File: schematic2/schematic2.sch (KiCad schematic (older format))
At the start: 47 parts, among them J1 Barrel_Jack, K1 TIANBO_HJR_1-2C, P1 Conn_02x20_Odd_Even, Q1 BC547, Q2 DMP1045U, Q3 BC547, Q4 BC547, Q5 BC547, U1 buck, U3 LM317_SOT-223

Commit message: Remove un-needed FET.
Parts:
- removed Q2: DMP1045U, Package_TO_SOT_SMD:SOT-23, symbol Device:Q_PMOS_GDS
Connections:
- wire segments 187 -> 182
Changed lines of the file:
@@
 	1    0    0    -1
 $EndComp
-Wire Wire Line
-	5850 3100 5950 3100
 $Comp
 L Mikes:buck U1
@@
 	1    0    0    -1
 $EndComp
-Wire Wire Line
-	6150 2800 6150 1350
-Wire Wire Line
-	6150 1350 4400 1350
-Wire Wire Line
-	4400 1350 4400 1650
-Connection ~ 4400 1650
-Wire Wire Line
-	4400 1650 4650 1650
-$Comp
-L Device:Q_PMOS_GDS Q2
-U 1 1 5F0952D9
-P 6150 3000
-F 0 "Q2" V 6399 2797 50  0000 L CNN
-F 1 "DMP1045U" V 6490 2797 50  0000 L CNN
-F 2 "Package_TO_SOT_SMD:SOT-23" H 6350 3100 50  0001 C CNN
-F 3 "~" H 6150 3000 50  0001 C CNN
-	1    6150 3000
-	0    -1   1    0
-$EndComp
 $Comp
 L Regulator_Linear:LM317_SOT-223 U?
@@
 	4150 3100 4150 3050
 Wire Wire Line
-	6350 3100 6700 3100
-Wire Wire Line
 	4950 1650 6300 1650
 Connection ~ 2650 1650
-Wire Wire Line
-	2650 1650 4400 1650
 $Comp
 L Diode:1N4001 D15
@@
 Wire Wire Line
 	4450 3550 4800 3550
+Wire Wire Line
+	5850 3100 6700 3100
+Wire Wire Line
+	2650 1650 4650 1650
 $EndSCHEMATC

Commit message: Boards ordered.
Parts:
- added J2: Conn_01x02, Connector_Molex:Molex_KK-254_AE-6410-02A_1x02_P2.54mm_Vertical, symbol Connector_Generic:Conn_01x02
- added R16: 1K, Resistor_THT:R_Axial_DIN0204_L3.6mm_D1.6mm_P5.08mm_Horizontal, symbol Device:R
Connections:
- net GND: now also J2.1 (Pin_1)
- net GPIO17(GEN0) renamed GPIO17
- net GPIO17: now also R16.1
- new net: J2.2 (Pin_2), R16.2
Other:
- note added: "POTENTIALLY USEFUL\nBUTTON ? :)"
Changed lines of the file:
@@
 Sheet 1 2
 Title "LiPo Pi UPS"
-Date "2020-06-03"
-Rev "2 DEV"
+Date "2021-08-11"
+Rev "3"
 Comp "MILLSTREAM COMPUTING"
 Comment1 ""
@@
 Wire Notes Line
 	3350 3900 3350 6200
-Wire Notes Line
-	3350 6200 9150 6200
-Wire Notes Line
-	9150 6200 9150 3900
-Wire Notes Line
-	9150 3900 3350 3900
 Text Notes 3400 4000 0    50   ~ 0
 Power Fail Detection
@@
 	6000 1500 6000 3450
 Wire Notes Line
-	6000 3450 9300 3450
-Wire Notes Line
 	9300 3450 9300 1500
 Wire Notes Line
@@
 Wire Wire Line
 	2650 1650 4650 1650
+Wire Notes Line
+	3350 3900 7100 3900
+Wire Notes Line
+	7100 3900 7100 6200
+Wire Notes Line
+	7100 6200 3350 6200
+Wire Notes Line
+	6000 3450 7250 3450
+Wire Notes Line
+	7250 3450 7250 4950
+Wire Notes Line
+	7250 4950 9900 4950
+Wire Notes Line
+	9900 4950 9900 3450
+Wire Notes Line
+	9900 3450 9300 3450
+Text GLabel -4300 3300 0    50   Input ~ 0
+GPIO17
+Text GLabel 10000 5550 2    50   Input ~ 0
+GPIO17
+$Comp
+L Connector_Generic:Conn_01x02 J2
+U 1 1 611A8E2F
+P 9250 5650
+F 0 "J2" H 9168 5325 50  0000 C CNN
+F 1 "Conn_01x02" H 9168 5416 50  0000 C CNN
+F 2 "Connector_Molex:Molex_KK-254_AE-6410-02A_1x02_P2.54mm_Vertical" H 9250 5650 50  0001 C CNN
+F 3 "~" H 9250 5650 50  0001 C CNN
+	1    9250 5650
+	-1   0    0    1
+$EndComp
+$Comp
+L power:GND #PWR0104
+U 1 1 611A94D4
+P 9450 5850
+F 0 "#PWR0104" H 9450 5600 50  0001 C CNN
+F 1 "GND" H 9450 5700 50  0000 C CNN
+F 2 "" H 9450 5850 50  0001 C CNN
+F 3 "" H 9450 5850 50  0001 C CNN
+	1    9450 5850
+	1    0    0    -1
+$EndComp
+$Comp
+L Device:R R16
+U 1 1 611A9DB8
+P 9750 5550
+F 0 "R16" V 9830 5550 50  0000 C CNN
+F 1 "1K" V 9750 5550 50  0000 C CNN
+F 2 "Resistor_THT:R_Axial_DIN0204_L3.6mm_D1.6mm_P5.08mm_Horizontal" V 9680 5550 50  0001 C CNN
+F 3 "" H 9750 5550 50  0001 C CNN
+	1    9750 5550
+	0    1    1    0
+$EndComp
+Wire Wire Line
+	9450 5550 9600 5550
+Wire Wire Line
+	9900 5550 10000 5550
+Wire Wire Line
+	9450 5650 9450 5850
+Text Notes 9600 5850 0    50   ~ 0
+POTENTIALLY USEFUL\nBUTTON ? :)
 $EndSCHEMATC

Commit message: Detail changes made from release note.
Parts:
- removed D14: 1N4001, Diode_SMD:D_2010_5025Metric, symbol Diode:1N4001
- removed K1: TIANBO_HJR_1-2C, Mikee:Relay_DPDT_HJR_1-2C, symbol Mikes:TIANBO_HJR_1-2C
- added Q2: FDS9435A, Package_SO:SOIC-8_3.9x4.9mm_P1.27mm, symbol Transistor_FET:FDS9435A
- added R17: 10K, Resistor_THT:R_Axial_DIN0204_L3.6mm_D1.6mm_P5.08mm_Horizontal, symbol Device:R
- BT1, BT2: value Battery_Cell -> 302323 LiPo
- C3: footprint Capacitor_SMD:C_0805_2012Metric -> Capacitor_SMD:C_1206_3216Metric
- D12: footprint Resistor_THT:R_Axial_DIN0207_L6.3mm_D2.5mm_P7.62mm_Horizontal -> Diode_THT:D_A-405_P7.62mm_Horizontal
- D3: value 5V6 -> 5V1
- D9: value 1N4001 -> 1N4148; footprint Diode_SMD:D_2010_5025Metric -> Diode_THT:D_DO-41_SOD81_P7.62mm_Horizontal
- R15: value 320R -> 310R
- R6: value 8K2 -> 10K
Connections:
- net +5V: no longer D9.1 (K)
- net at D11.1 (K), Q4.1 (C): now also Q2.4 (G), R17.2; no longer D9.2 (A)
- net at D7.1 (K): now also Q2.1 (S), Q2.2 (S), Q2.3 (S), R17.1
- net at D5.1 (K), U1.1 (V+in): now also Q2.5 (D), Q2.6 (D), Q2.7 (D), Q2.8 (D)
- net at C1.1, U3.3 (VI): now also D9.1 (K)
- net +9V renamed +12V
- net +12V: now also D9.2 (A)
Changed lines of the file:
@@
 Sheet 1 2
 Title "LiPo Pi UPS"
-Date "2021-08-11"
-Rev "3"
+Date "2022-04-04"
+Rev "3.1"
 Comp "MILLSTREAM COMPUTING"
-Comment1 ""
-Comment2 ""
+Comment1 "NOT FOR MANUFACTURE"
+Comment2 "SEE HW RELEASE NOT 101 FOR V3 FOR CHANGES"
 Comment3 ""
 Comment4 ""
@@
 $EndComp
 $Comp
-L power:+9V #PWR06
-U 1 1 5B3B4742
-P 1800 1350
-F 0 "#PWR06" H 1800 1200 50  0001 C CNN
-F 1 "+9V" H 1800 1490 50  0000 C CNN
-F 2 "" H 1800 1350 50  0001 C CNN
-F 3 "" H 1800 1350 50  0001 C CNN
-	1    1800 1350
-	1    0    0    -1
-$EndComp
-$Comp
-L Diode:1N4001 D9
-U 1 1 5B3B47EF
-P 7900 2750
-F 0 "D9" H 7900 2850 50  0000 C CNN
-F 1 "1N4001" H 7900 2650 50  0000 C CNN
-F 2 "Diode_SMD:D_2010_5025Metric" H 7900 2575 50  0001 C CNN
-F 3 "" H 7900 2750 50  0001 C CNN
-	1    7900 2750
-	0    1    1    0
-$EndComp
-$Comp
 L Diode:1N4001 D7
 U 1 1 5B3B494C
@@
 P 4600 5800
 F 0 "R6" V 4680 5800 50  0000 C CNN
-F 1 "8K2" V 4600 5800 50  0000 C CNN
+F 1 "10K" V 4600 5800 50  0000 C CNN
 F 2 "Resistor_THT:R_Axial_DIN0204_L3.6mm_D1.6mm_P5.08mm_Horizontal" V 4530 5800 50  0001 C CNN
 F 3 "" H 4600 5800 50  0001 C CNN
@@
 	1700 1850 1700 2050
 Connection ~ 1800 1650
-Wire Wire Line
-	6300 2450 6300 1650
 $Comp
 L power:GND #PWR09
@@
 $EndComp
 Wire Wire Line
-	7700 1650 7700 2450
-Wire Wire Line
-	7700 2450 7500 2450
-Wire Wire Line
-	7700 2450 7900 2450
-Wire Wire Line
-	7900 2450 7900 2600
-Connection ~ 7700 2450
-Wire Wire Line
-	7500 3050 7500 3200
-Wire Wire Line
-	7500 3200 7900 3200
-Wire Wire Line
-	7900 3200 7900 2900
-Connection ~ 7500 3200
-Wire Wire Line
-	7500 3200 7500 3500
-Wire Wire Line
 	8200 4250 7800 4250
 Wire Wire Line
@@
 Wire Wire Line
 	7500 6050 7500 6250
-Wire Wire Line
-	7700 1650 8300 1650
 Wire Wire Line
 	10350 1650 10350 1250
@@
 P 2100 3400
 F 0 "D3" H 2100 3500 50  0000 C CNN
-F 1 "5V6" H 2100 3300 50  0000 C CNN
+F 1 "5V1" H 2100 3300 50  0000 C CNN
 F 2 "Diode_THT:D_A-405_P7.62mm_Horizontal" H 2100 3400 50  0001 C CNN
 F 3 "~" H 2100 3400 50  0001 C CNN
@@
 Connection ~ 6300 1650
 Wire Wire Line
-	7450 1650 7700 1650
-Wire Wire Line
 	6700 1950 6700 2050
-Connection ~ 7700 1650
 Text Notes 5400 4750 0    50   ~ 0
 0=OK, 1=POWER FAIL
@@
 Text Notes 1950 3750 1    50   ~ 0
 POWER INDICATOR
-Text Notes 8350 2900 0    50   ~ 0
+Text Notes 8450 3100 0    50   ~ 0
 UPS ACTIVE\nINDICATOR
 Text Notes 6250 4450 0    50   ~ 0
@@
 F 0 "C3" H 4565 2796 50  0000 L CNN
 F 1 "100n" H 4565 2705 50  0000 L CNN
-F 2 "Capacitor_SMD:C_0805_2012Metric" H 4488 2600 50  0001 C CNN
+F 2 "Capacitor_SMD:C_1206_3216Metric" H 4488 2600 50  0001 C CNN
 F 3 "~" H 4450 2750 50  0001 C CNN
 	1    4450 2750
@@
 AR Path="/5F2C0373" Ref="BT1"  Part="1"
 F 0 "BT1" H 5268 2596 50  0000 L CNN
-F 1 "Battery_Cell" H 5268 2505 50  0000 L CNN
+F 1 "302323 LiPo" H 5268 2505 50  0000 L CNN
 F 2 "Connector_Molex:Molex_KK-254_AE-6410-02A_1x02_P2.54mm_Vertical" V 5150 2560 50  0001 C CNN
 F 3 "~" V 5150 2560 50  0001 C CNN
@@
 AR Path="/5F2C0379" Ref="BT2"  Part="1"
 F 0 "BT2" H 5268 3396 50  0000 L CNN
-F 1 "Battery_Cell" H 5268 3305 50  0000 L CNN
+F 1 "302323 LiPo" H 5268 3305 50  0000 L CNN
 F 2 "Connector_Molex:Molex_KK-254_AE-6410-02A_1x02_P2.54mm_Vertical" V 5150 3360 50  0001 C CNN
 F 3 "~" V 5150 3360 50  0001 C CNN
@@
 F 0 "D12" V 4754 3202 50  0000 C CNN
 F 1 "3V6" V 4845 3202 50  0000 C CNN
-F 2 "Resistor_THT:R_Axial_DIN0207_L6.3mm_D2.5mm_P7.62mm_Horizontal" H 4800 3050 50  0001 C CNN
+F 2 "Diode_THT:D_A-405_P7.62mm_Horizontal" H 4800 3050 50  0001 C CNN
 F 3 "~" H 4800 3050 50  0001 C CNN
 	1    4800 3050
@@
 Connection ~ 2800 2150
 Wire Wire Line
-	2100 1650 2650 1650
-Wire Wire Line
 	2100 6050 3800 6050
-Wire Wire Line
-	2650 1650 2650 1750
 Wire Wire Line
 	5150 3550 5550 3550
@@
 AR Path="/5F3B4ACA" Ref="R15"  Part="1"
 F 0 "R15" H 4319 3296 50  0000 C CNN
-F 1 "320R" H 4319 3205 50  0000 C CNN
+F 1 "310R" H 4319 3205 50  0000 C CNN
 F 2 "Resistor_THT:R_Axial_DIN0204_L3.6mm_D1.6mm_P5.08mm_Horizontal" V 4080 3250 50  0001 C CNN
 F 3 "~" H 4150 3250 50  0001 C CNN
@@
 Wire Wire Line
 	4950 1650 6300 1650
-Connection ~ 2650 1650
 $Comp
 L Diode:1N4001 D15
@@
 Wire Wire Line
 	5850 3550 6000 3550
-$Comp
-L Diode:1N4001 D14
-U 1 1 5F3EA42D
-P 2650 1900
-F 0 "D14" H 2650 2000 50  0000 C CNN
-F 1 "1N4001" H 2650 1800 50  0000 C CNN
-F 2 "Diode_SMD:D_2010_5025Metric" H 2650 1725 50  0001 C CNN
-F 3 "" H 2650 1900 50  0001 C CNN
-	1    2650 1900
-	0    -1   -1   0
-$EndComp
-Wire Wire Line
-	2650 2050 2650 2150
-$Comp
-L Mikes:TIANBO_HJR_1-2C K1
-U 1 1 5F44ADD7
-P 7300 2750
-F 0 "K1" H 6181 2796 50  0000 L CNN
-F 1 "TIANBO_HJR_1-2C" H 6181 2705 50  0000 L CNN
-F 2 "Mikee:Relay_DPDT_HJR_1-2C" H 8850 2720 50  0001 C CNN
-F 3 "" H 7300 2750 50  0001 C CNN
-	1    7300 2750
-	-1   0    0    -1
-$EndComp
+Wire Wire Line
+	2650 1650 2650 1750
 Wire Wire Line
 	6300 2450 6600 2450
 Wire Wire Line
-	6700 3050 6700 3100
+	6600 2850 6600 3100
 Text GLabel 2750 6650 2    50   Input ~ 0
 CLK_BAT
@@
 	4450 3550 4800 3550
 Wire Wire Line
-	5850 3100 6700 3100
-Wire Wire Line
-	2650 1650 4650 1650
+	5850 3100 6150 3100
 Wire Notes Line
 	3350 3900 7100 3900
@@
 Text Notes 9600 5850 0    50   ~ 0
 POTENTIALLY USEFUL\nBUTTON ? :)
+Wire Wire Line
+	2100 1650 2650 1650
+Connection ~ 2650 1650
+Wire Wire Line
+	2650 1650 4650 1650
+$Comp
+L power:+12V #PWR0105
+U 1 1 624FAA52
+P 1800 1350
+F 0 "#PWR0105" H 1800 1200 50  0001 C CNN
+F 1 "+12V" H 1800 1490 50  0000 C CNN
+F 2 "" H 1800 1350 50  0001 C CNN
+F 3 "" H 1800 1350 50  0001 C CNN
+	1    1800 1350
+	1    0    0    -1
+$EndComp
+$Comp
+L Transistor_FET:FDS9435A Q2
+U 1 1 62504EB3
+P 6500 2650
+F 0 "Q2" H 6700 2725 50  0000 L CNN
+F 1 "FDS9435A" H 6700 2650 50  0000 L CNN
+F 2 "Package_SO:SOIC-8_3.9x4.9mm_P1.27mm" H 6700 2575 50  0001 L CIN
+F 3 "https://www.onsemi.com/pub/Collateral/FDS9435A-D.PDF" V 6500 2650 50  0001 L CNN
+	1    6500 2650
+	1    0    0    -1
+$EndComp
+Wire Wire Line
+	6300 2650 6300 2900
+Wire Wire Line
+	6300 2900 7500 2900
+Wire Wire Line
+	7500 2900 7500 3500
+Wire Wire Line
+	7450 1650 8300 1650
+$Comp
+L Device:R R17
+U 1 1 6252D92A
+P 6150 2800
+F 0 "R17" V 6250 2800 50  0000 C CNN
+F 1 "10K" V 6150 2800 50  0000 C CNN
+F 2 "Resistor_THT:R_Axial_DIN0204_L3.6mm_D1.6mm_P5.08mm_Horizontal" V 6080 2800 50  0001 C CNN
+F 3 "" H 6150 2800 50  0001 C CNN
+	1    6150 2800
+	-1   0    0    1
+$EndComp
+Wire Wire Line
+	6300 1650 6300 2450
+Wire Wire Line
+	6150 2950 6150 3100
+Connection ~ 6150 3100
+Wire Wire Line
+	6150 3100 6600 3100
+Wire Wire Line
+	6300 2650 6150 2650
+Connection ~ 6300 2650
+$Comp
+L Diode:1N4001 D9
+U 1 1 625B6ABC
+P 2650 1900
+F 0 "D9" H 2650 2000 50  0000 C CNN
+F 1 "1N4148" H 2650 1800 50  0000 C CNN
+F 2 "Diode_THT:D_DO-41_SOD81_P7.62mm_Horizontal" H 2650 1725 50  0001 C CNN
+F 3 "" H 2650 1900 50  0001 C CNN
+	1    2650 1900
+	0    -1   -1   0
+$EndComp
+Wire Wire Line
+	2650 2050 2650 2150
 $EndSCHEMATC

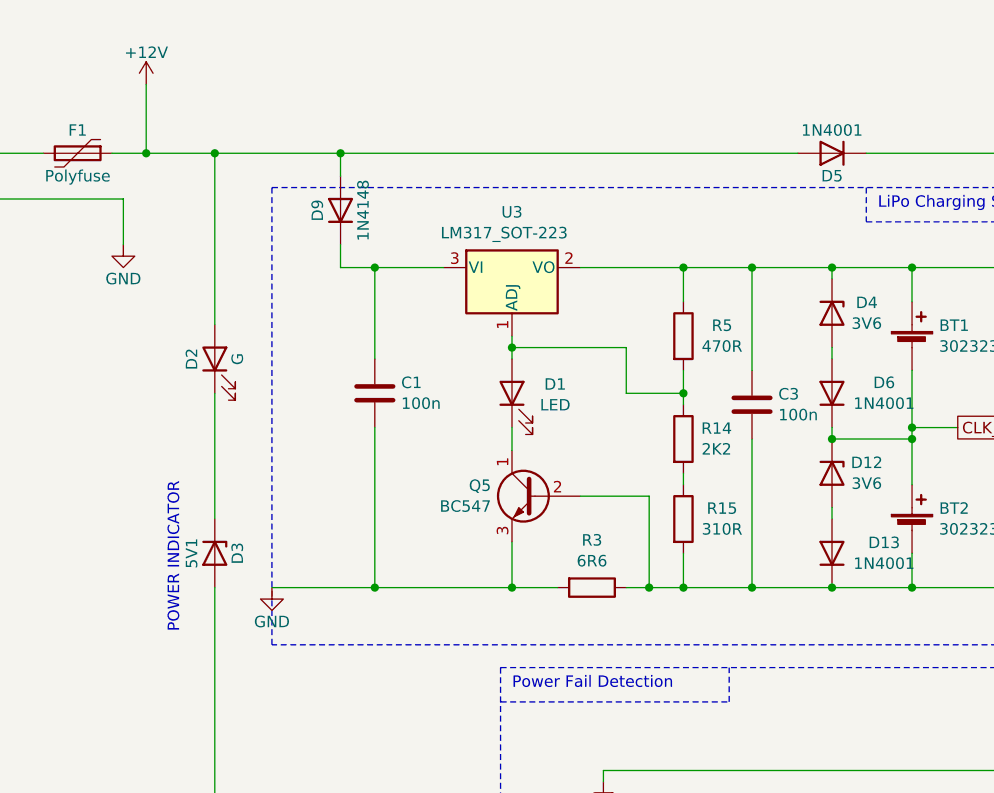
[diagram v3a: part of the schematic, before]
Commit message: Better view of amended assembly.
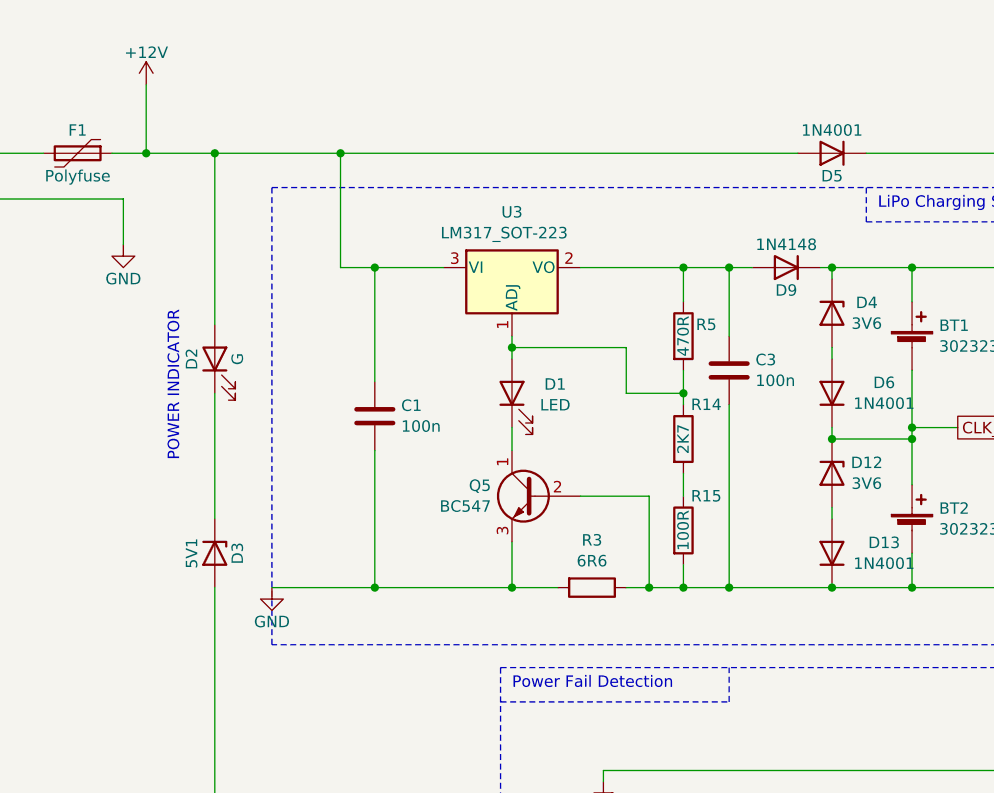
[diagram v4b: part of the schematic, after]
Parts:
- R14: value 2K2 -> 2K7
- R15: value 310R -> 100R
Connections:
- net +12V: now also C1.1, U3.3 (VI); no longer D9.2 (A)
- net at BT1.1 (+), D4.1 (K), D7.2 (A): now also D9.1 (K); no longer C3.1, R5.1, U3.2 (VO)
- new net: C3.1, D9.2 (A), R5.1, U3.2 (VO)
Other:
- moved on the sheet: C1, C3, D9
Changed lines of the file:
@@
 Wire Wire Line
 	8950 4250 9500 4250
-Text Notes 1950 3750 1    50   ~ 0
+Text Notes 1950 3000 1    50   ~ 0
 POWER INDICATOR
 Text Notes 8450 3100 0    50   ~ 0
@@
 AR Path="/5F26DD5A/5F2C033A" Ref="R?"  Part="1"
 AR Path="/5F2C033A" Ref="R5"  Part="1"
-F 0 "R5" H 4319 2496 50  0000 C CNN
-F 1 "470R" H 4319 2405 50  0000 C CNN
+F 0 "R5" H 4250 2500 50  0000 C CNN
+F 1 "470R" V 4150 2450 50  0000 C CNN
 F 2 "Resistor_THT:R_Axial_DIN0204_L3.6mm_D1.6mm_P5.08mm_Horizontal" V 4080 2450 50  0001 C CNN
 F 3 "~" H 4150 2450 50  0001 C CNN
@@
 AR Path="/5F26DD5A/5F2C0340" Ref="R?"  Part="1"
 AR Path="/5F2C0340" Ref="R14"  Part="1"
-F 0 "R14" H 4295 2946 50  0000 C CNN
-F 1 "2K2" H 4295 2855 50  0000 C CNN
+F 0 "R14" H 4250 3050 50  0000 C CNN
+F 1 "2K7" V 4150 2900 50  0000 C CNN
 F 2 "Resistor_THT:R_Axial_DIN0204_L3.6mm_D1.6mm_P5.08mm_Horizontal" V 4080 2900 50  0001 C CNN
 F 3 "~" H 4150 2900 50  0001 C CNN
@@
 Wire Wire Line
 	4000 3550 4150 3550
-Wire Wire Line
-	4150 3550 4150 3400
 Connection ~ 4000 3550
 Wire Wire Line
@@
 $Comp
 L Device:C C?
-U 1 1 5F2C0367
-P 2800 2700
-AR Path="/5F26DD5A/5F2C0367" Ref="C?"  Part="1"
-AR Path="/5F2C0367" Ref="C1"  Part="1"
-F 0 "C1" H 2915 2746 50  0000 L CNN
-F 1 "100n" H 2915 2655 50  0000 L CNN
-F 2 "Capacitor_THT:C_Disc_D4.3mm_W1.9mm_P5.00mm" H 2838 2550 50  0001 C CNN
-F 3 "~" H 2800 2700 50  0001 C CNN
-	1    2800 2700
-	1    0    0    -1
-$EndComp
-$Comp
-L Device:C C?
 U 1 1 5F2C036D
-P 4450 2750
+P 4350 2600
 AR Path="/5F26DD5A/5F2C036D" Ref="C?"  Part="1"
 AR Path="/5F2C036D" Ref="C3"  Part="1"
-F 0 "C3" H 4565 2796 50  0000 L CNN
-F 1 "100n" H 4565 2705 50  0000 L CNN
-F 2 "Capacitor_SMD:C_1206_3216Metric" H 4488 2600 50  0001 C CNN
-F 3 "~" H 4450 2750 50  0001 C CNN
-	1    4450 2750
+F 0 "C3" H 4465 2646 50  0000 L CNN
+F 1 "100n" H 4465 2555 50  0000 L CNN
+F 2 "Capacitor_SMD:C_1206_3216Metric" H 4388 2450 50  0001 C CNN
+F 3 "~" H 4350 2600 50  0001 C CNN
+	1    4350 2600
 	1    0    0    -1
 $EndComp
@@
 $EndComp
 Wire Wire Line
-	4150 2150 4450 2150
+	4150 2150 4350 2150
 Wire Wire Line
 	5150 2150 5150 2300
@@
 	5150 3550 4800 3550
 Connection ~ 4150 3550
-Connection ~ 4450 2150
+Connection ~ 4350 2150
 Wire Wire Line
 	3100 2150 2800 2150
 Wire Wire Line
-	2800 2150 2800 2550
-Wire Wire Line
-	2800 2850 2800 3550
+	2800 2950 2800 3550
 Wire Wire Line
 	2350 3550 2800 3550
@@
 	5150 2900 5150 3100
 Wire Wire Line
-	4800 2550 4800 2500
-Wire Wire Line
-	4800 3200 4800 3250
-Wire Wire Line
 	4800 2200 4800 2150
 Connection ~ 4800 2150
@@
 	5550 2150 5550 3100
 Connection ~ 5150 2150
-$Comp
-L Device:R R?
-U 1 1 5F3B4ACA
-P 4150 3250
-AR Path="/5F26DD5A/5F3B4ACA" Ref="R?"  Part="1"
-AR Path="/5F3B4ACA" Ref="R15"  Part="1"
-F 0 "R15" H 4319 3296 50  0000 C CNN
-F 1 "310R" H 4319 3205 50  0000 C CNN
-F 2 "Resistor_THT:R_Axial_DIN0204_L3.6mm_D1.6mm_P5.08mm_Horizontal" V 4080 3250 50  0001 C CNN
-F 3 "~" H 4150 3250 50  0001 C CNN
-	1    4150 3250
-	1    0    0    -1
-$EndComp
-Wire Wire Line
-	4150 3100 4150 3050
 Wire Wire Line
 	4950 1650 6300 1650
@@
 	5850 3550 6000 3550
 Wire Wire Line
-	2650 1650 2650 1750
-Wire Wire Line
 	6300 2450 6600 2450
 Wire Wire Line
@@
 	9300 1500 6000 1500
 Wire Wire Line
-	4150 3550 4450 3550
-Wire Wire Line
-	4450 2150 4450 2600
-Wire Wire Line
-	4450 2150 4800 2150
-Wire Wire Line
-	4450 2900 4450 3550
-Connection ~ 4450 3550
-Wire Wire Line
-	4450 3550 4800 3550
+	4150 3550 4350 3550
+Wire Wire Line
+	4350 2150 4350 2450
+Wire Wire Line
+	4350 2150 4450 2150
+Wire Wire Line
+	4350 2750 4350 3550
+Connection ~ 4350 3550
+Wire Wire Line
+	4350 3550 4800 3550
 Wire Wire Line
 	5850 3100 6150 3100
@@
 L Diode:1N4001 D9
 U 1 1 625B6ABC
-P 2650 1900
-F 0 "D9" H 2650 2000 50  0000 C CNN
-F 1 "1N4148" H 2650 1800 50  0000 C CNN
-F 2 "Diode_THT:D_DO-41_SOD81_P7.62mm_Horizontal" H 2650 1725 50  0001 C CNN
-F 3 "" H 2650 1900 50  0001 C CNN
-	1    2650 1900
-	0    -1   -1   0
-$EndComp
-Wire Wire Line
-	2650 2050 2650 2150
+P 4600 2150
+F 0 "D9" H 4600 2250 50  0000 C CNN
+F 1 "1N4148" H 4600 2050 50  0000 C CNN
+F 2 "Diode_THT:D_DO-41_SOD81_P7.62mm_Horizontal" H 4600 1975 50  0001 C CNN
+F 3 "" H 4600 2150 50  0001 C CNN
+	1    4600 2150
+	-1   0    0    1
+$EndComp
+Wire Wire Line
+	4750 2150 4800 2150
+Wire Wire Line
+	2650 1650 2650 2150
+Wire Wire Line
+	4150 3050 4150 3150
+$Comp
+L Device:R R?
+U 1 1 624E119B
+P 4150 3300
+AR Path="/5F26DD5A/624E119B" Ref="R?"  Part="1"
+AR Path="/624E119B" Ref="R15"  Part="1"
+F 0 "R15" H 4250 3450 50  0000 C CNN
+F 1 "100R" V 4150 3300 50  0000 C CNN
+F 2 "Resistor_THT:R_Axial_DIN0204_L3.6mm_D1.6mm_P5.08mm_Horizontal" V 4080 3300 50  0001 C CNN
+F 3 "~" H 4150 3300 50  0001 C CNN
+	1    4150 3300
+	1    0    0    -1
+$EndComp
+Wire Wire Line
+	4150 3450 4150 3550
+Wire Wire Line
+	4800 2550 4800 2500
+Wire Wire Line
+	4800 3200 4800 3250
+Wire Wire Line
+	2800 2150 2800 2650
+$Comp
+L Device:C C?
+U 1 1 5F2C0367
+P 2800 2800
+AR Path="/5F26DD5A/5F2C0367" Ref="C?"  Part="1"
+AR Path="/5F2C0367" Ref="C1"  Part="1"
+F 0 "C1" H 2915 2846 50  0000 L CNN
+F 1 "100n" H 2915 2755 50  0000 L CNN
+F 2 "Capacitor_THT:C_Disc_D4.3mm_W1.9mm_P5.00mm" H 2838 2650 50  0001 C CNN
+F 3 "~" H 2800 2800 50  0001 C CNN
+	1    2800 2800
+	1    0    0    -1
+$EndComp
 $EndSCHEMATC
